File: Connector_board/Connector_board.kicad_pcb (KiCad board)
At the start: 2 copper layers, 54.2 x 20 mm, 7 parts, among them J1 SM03B-SRSS-TB, J2 USB_B_Micro, J3 Conn_02x06_Odd_Even, J5 Conn_02x06_Top_Bottom, J6 Conn_02x06_Top_Bottom

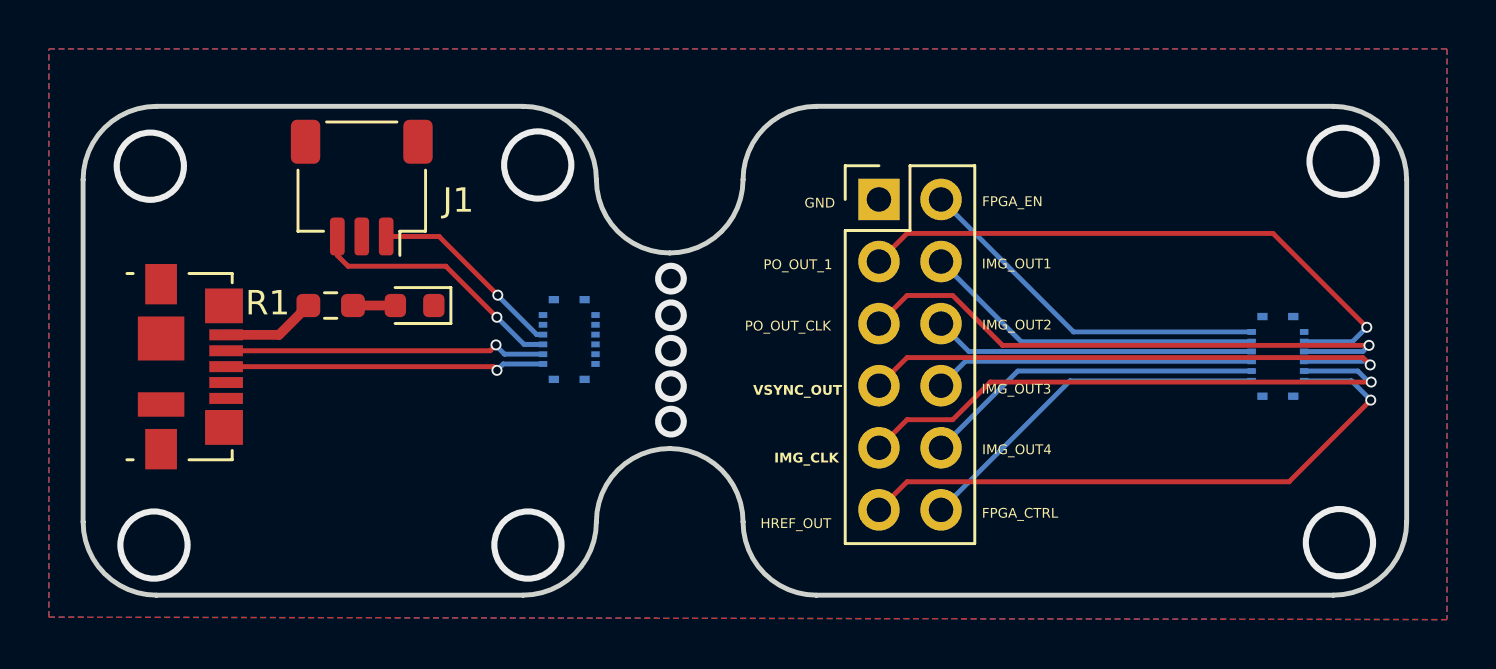
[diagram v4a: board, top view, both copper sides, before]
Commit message: connector board layout tweaked
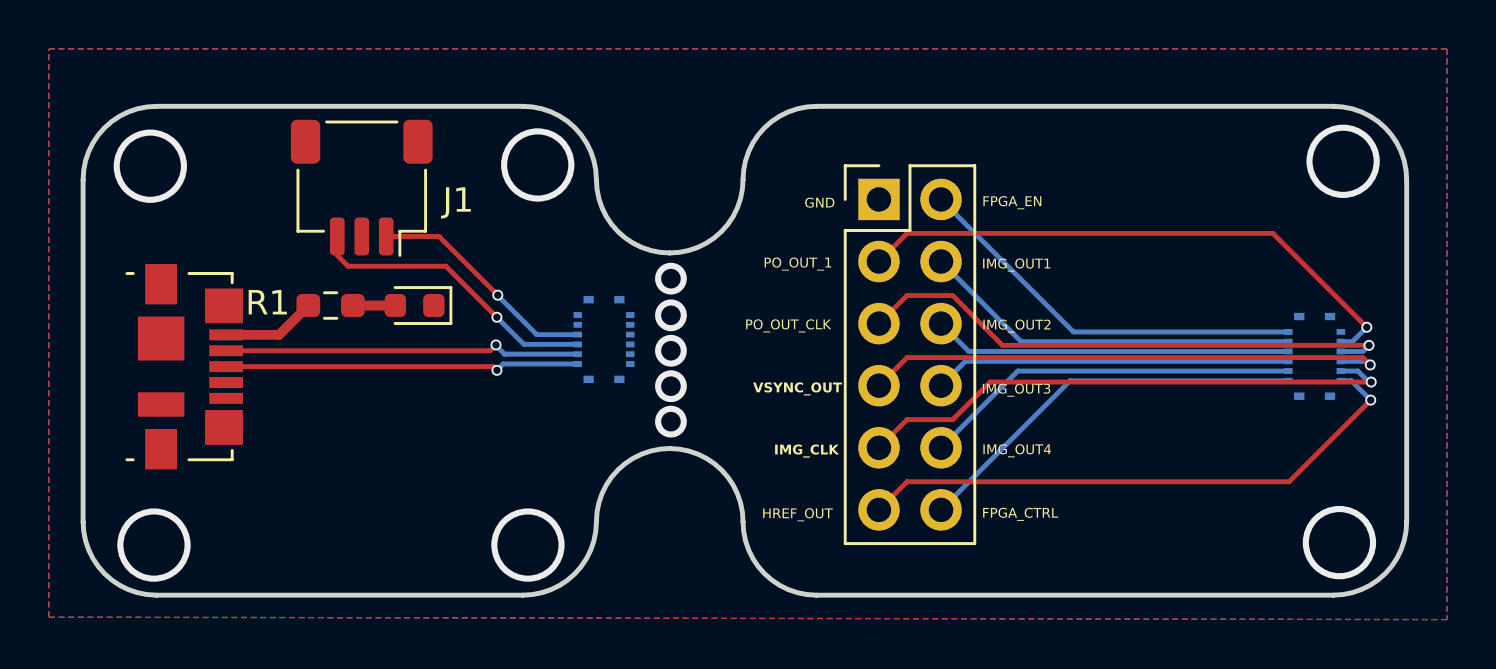
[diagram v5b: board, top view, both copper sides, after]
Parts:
- moved J5 1.50 mm to (65.7, 42.9)
- moved J6 1.42 mm to (36.6, 42.2)
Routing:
- net /POSITION_OUT_CLK: track 24.1 -> 22.6 mm
- net /POSITION_OUT_1: track 24.8 -> 23.3 mm
- net /IMAGE_CLK: track 24.2 -> 22.7 mm
- net /HREF_OUT: track 25.0 -> 23.5 mm
- net /FPGA_CTRL: track 14.9 -> 16.4 mm
- net /IMAGE_OUT_4: track 14.0 -> 15.5 mm
- net /IMAGE_OUT_3: track 13.1 -> 14.6 mm
- net /IMAGE_OUT_2: track 13.2 -> 14.7 mm
- net /IMAGE_OUT_1: track 14.1 -> 15.6 mm
- net /FPGA_EN: track 15.0 -> 16.5 mm
- net /VSYNC_OUT: track 23.4 -> 22.0 mm
- net /USB_D1-: track 13.2 -> 14.6 mm
- net /USB_D1+: track 13.1 -> 14.6 mm
- net /SWD_1: track 8.54 -> 9.96 mm
- net /SWCLK_1: track 10.7 -> 12.1 mm
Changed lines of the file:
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@@
 	(footprint "5035521222:CON_5035521222"
 		(layer "B.Cu")
-		(at 64.18 42.93 90)
+		(at 65.685 42.93 90)
 		(property "Reference" "J5"
 			(at -0.1016 5.08 90)
@@
 	(footprint "5035521222:CON_5035521222"
 		(layer "B.Cu")
-		(at 35.19 42.24 90)
+		(at 36.61 42.24 90)
 		(property "Reference" "J6"
 			(at -0.1016 5.08 90)
@@
 	)
 	(gr_text "PO_OUT_CLK"
-		(at 42.37 41.92 0)
+		(at 42.37 41.87 0)
 		(layer "F.SilkS")
 		(effects
@@
 	)
 	(gr_text "HREF_OUT"
-		(at 43.01 50 0)
+		(at 43.07 49.6 0)
 		(layer "F.SilkS")
 		(effects
@@
 	)
 	(gr_text "PO_OUT_1"
-		(at 43.13 39.41 0)
+		(at 43.13 39.34 0)
 		(layer "F.SilkS")
 		(effects
@@
 	)
 	(gr_text "VSYNC_OUT"
-		(at 42.71 44.55 0)
+		(at 42.71 44.45 0)
 		(layer "F.SilkS")
 		(effects
@@
 	)
 	(gr_text "IMG_CLK"
-		(at 43.57 47.32 0)
+		(at 43.56 46.99 0)
 		(layer "F.SilkS")
 		(effects
@@
 	)
 	(segment
-		(start 34.115 42.04)
+		(start 35.535 42.04)
 		(end 33.86 42.04)
 		(width 0.2)
@@
 	)
 	(segment
-		(start 34.115 42.44)
+		(start 35.535 42.44)
 		(end 33.34 42.44)
 		(width 0.2)
@@
 	)
 	(segment
-		(start 63.105 41.93)
+		(start 64.61 41.93)
 		(end 55.82 41.93)
 		(width 0.2)
@@
 	)
 	(segment
-		(start 65.255 42.33)
-		(end 67.23 42.33)
+		(start 67.23 42.33)
+		(end 66.76 42.33)
 		(width 0.2)
 		(layer "B.Cu")
@@
 	)
 	(segment
+		(start 64.61 42.33)
+		(end 53.68 42.33)
+		(width 0.2)
+		(layer "B.Cu")
+		(net "/IMAGE_OUT_1")
+	)
+	(segment
 		(start 53.68 42.33)
 		(end 50.4 39.05)
-		(width 0.2)
-		(layer "B.Cu")
-		(net "/IMAGE_OUT_1")
-	)
-	(segment
-		(start 63.105 42.33)
-		(end 53.68 42.33)
 		(width 0.2)
 		(layer "B.Cu")
@@
 	)
 	(segment
-		(start 65.255 42.73)
-		(end 67.66 42.73)
+		(start 67.66 42.73)
+		(end 66.76 42.73)
 		(width 0.2)
 		(layer "B.Cu")
 		(net "/POSITION_OUT_CLK")
+	)
+	(segment
+		(start 64.61 42.73)
+		(end 51.54 42.73)
+		(width 0.2)
+		(layer "B.Cu")
+		(net "/IMAGE_OUT_2")
 	)
 	(segment
 		(start 51.54 42.73)
 		(end 50.4 41.59)
-		(width 0.2)
-		(layer "B.Cu")
-		(net "/IMAGE_OUT_2")
-	)
-	(segment
-		(start 63.105 42.73)
-		(end 51.54 42.73)
 		(width 0.2)
 		(layer "B.Cu")
@@
 	)
 	(segment
-		(start 67.8 43.13)
-		(end 67.94 43.27)
+		(start 67.81 43.13)
+		(end 66.76 43.13)
 		(width 0.2)
 		(layer "B.Cu")
@@
 	)
 	(segment
-		(start 65.255 43.13)
-		(end 67.8 43.13)
+		(start 67.96 43.28)
+		(end 67.81 43.13)
 		(width 0.2)
 		(layer "B.Cu")
 		(net "/VSYNC_OUT")
+	)
+	(segment
+		(start 64.61 43.13)
+		(end 51.4 43.13)
+		(width 0.2)
+		(layer "B.Cu")
+		(net "/IMAGE_OUT_3")
 	)
 	(segment
 		(start 51.4 43.13)
 		(end 50.4 44.13)
-		(width 0.2)
-		(layer "B.Cu")
-		(net "/IMAGE_OUT_3")
-	)
-	(segment
-		(start 63.105 43.13)
-		(end 51.4 43.13)
 		(width 0.2)
 		(layer "B.Cu")
@@
 	(segment
 		(start 67.45 43.53)
-		(end 65.255 43.53)
+		(end 66.76 43.53)
 		(width 0.2)
 		(layer "B.Cu")
@@
 	)
 	(segment
+		(start 64.61 43.53)
+		(end 53.54 43.53)
+		(width 0.2)
+		(layer "B.Cu")
+		(net "/IMAGE_OUT_4")
+	)
+	(segment
 		(start 53.54 43.53)
 		(end 50.4 46.67)
-		(width 0.2)
-		(layer "B.Cu")
-		(net "/IMAGE_OUT_4")
-	)
-	(segment
-		(start 63.105 43.53)
-		(end 53.54 43.53)
 		(width 0.2)
 		(layer "B.Cu")
@@
 	)
 	(segment
-		(start 65.255 43.93)
-		(end 67.19 43.93)
+		(start 67.19 43.93)
+		(end 66.76 43.93)
 		(width 0.2)
 		(layer "B.Cu")
@@
 	)
 	(segment
-		(start 63.105 43.93)
+		(start 64.61 43.93)
 		(end 55.68 43.93)
 		(width 0.2)
@@
 	)
 	(segment
+		(start 35.535 42.84)
+		(end 32.54 42.84)
+		(width 0.2)
+		(layer "B.Cu")
+		(net "/USB_D1-")
+	)
+	(segment
 		(start 32.54 42.84)
 		(end 32.18 42.48)
-		(width 0.2)
-		(layer "B.Cu")
-		(net "/USB_D1-")
-	)
-	(segment
-		(start 34.115 42.84)
-		(end 32.54 42.84)
 		(width 0.2)
 		(layer "B.Cu")
@@
 	)
 	(segment
-		(start 34.115 43.24)
+		(start 35.535 43.24)
 		(end 32.49 43.24)
 		(width 0.2)
@@
 			)
 		)
-	)
-	(zone
-		(layer "B.Cu")
-		(hatch edge 0.5)
-		(connect_pads
-			(clearance 0)
-		)
-		(min_thickness 0.25)
-		(keepout
-			(tracks allowed)
-			(vias allowed)
-			(pads allowed)
-			(copperpour not_allowed)
-			(footprints allowed)
-		)
-		(placement
-			(enabled no)
-			(sheetname "/")
-		)
-		(fill
-			(thermal_gap 0.5)
-			(thermal_bridge_width 0.5)
-			(island_removal_mode 0)
-		)
-		(polygon
-			(pts
-				(xy 75.376676 46.62) (xy 78.086676 46.6) (xy 78.116676 50.96) (xy 75.406676 50.96)
-			)
-		)
-	)
-	(zone
-		(layer "B.Cu")
-		(hatch edge 0.5)
-		(connect_pads
-			(clearance 0)
-		)
-		(min_thickness 0.25)
-		(keepout
-			(tracks allowed)
-			(vias allowed)
-			(pads allowed)
-			(copperpour not_allowed)
-			(footprints allowed)
-		)
-		(placement
-			(enabled no)
-			(sheetname "/")
-		)
-		(fill
-			(thermal_gap 0.5)
-			(thermal_bridge_width 0.5)
-			(island_removal_mode 0)
-		)
-		(polygon
-			(pts
-				(xy 39.43 58.49) (xy 42.14 58.47) (xy 42.17 62.83) (xy 39.46 62.83)
-			)
-		)
